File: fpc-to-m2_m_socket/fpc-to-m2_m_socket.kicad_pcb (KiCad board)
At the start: 6 copper layers, 99.3 x 40.6 mm, 31 parts, among them J2 Bus_M.2_Socket_M, J5 Conn_01x02_Pin, Y1 OK2EL89CJI-111YLC-32.768K

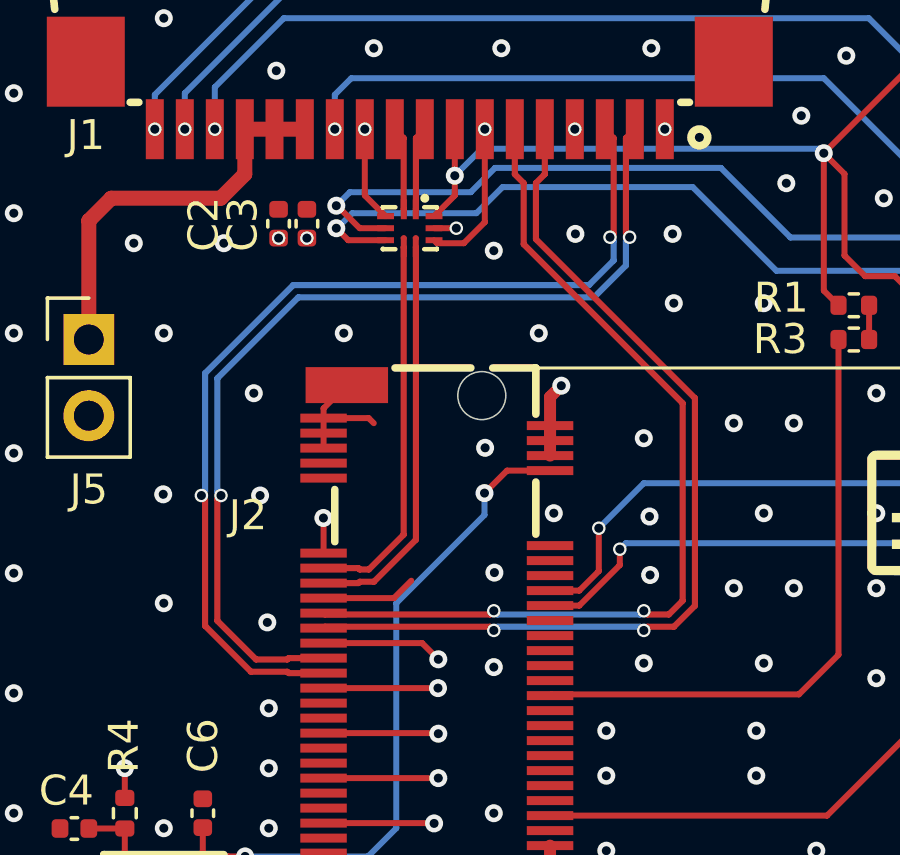
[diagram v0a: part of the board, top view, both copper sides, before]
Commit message: add fillets and skew tuning
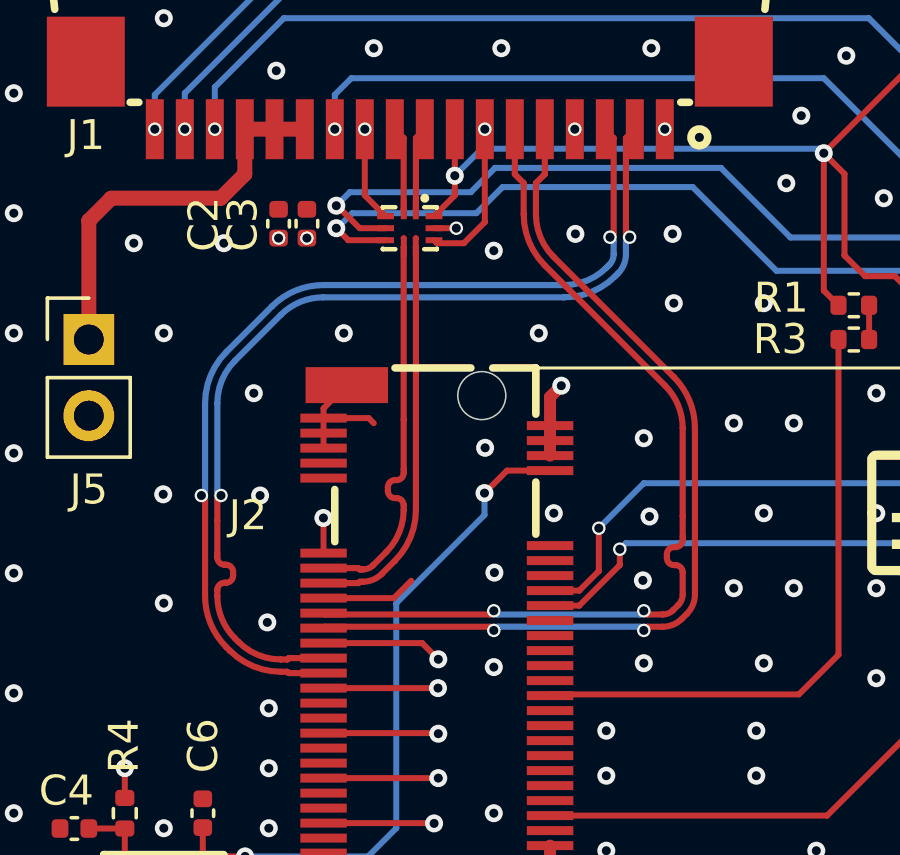
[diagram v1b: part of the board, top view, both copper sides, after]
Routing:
- net PCIe_RX-: track 32.9 -> 32.3 mm

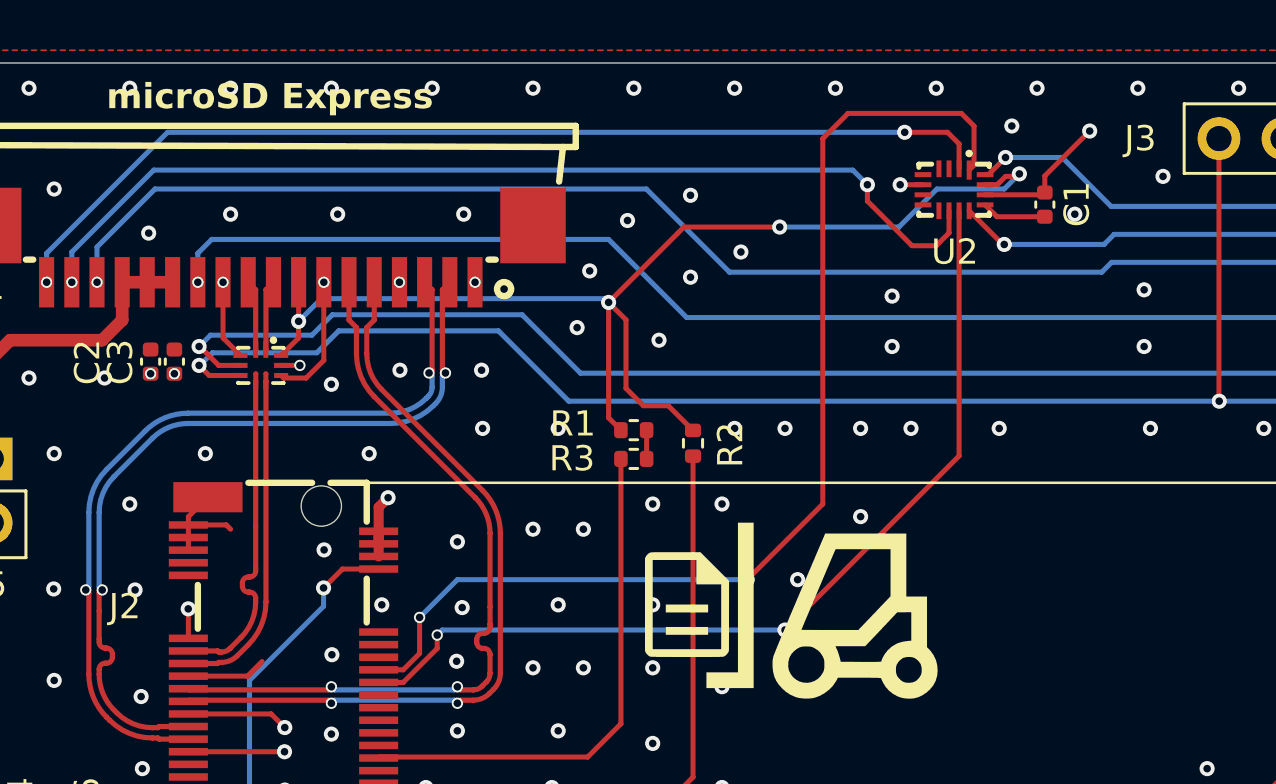
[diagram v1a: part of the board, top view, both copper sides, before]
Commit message: fpc-to-m2_m_socket: switch TMUX1574 to TSSOP-16
The UQFN-16 variant just went out of stock at jlcpcb.
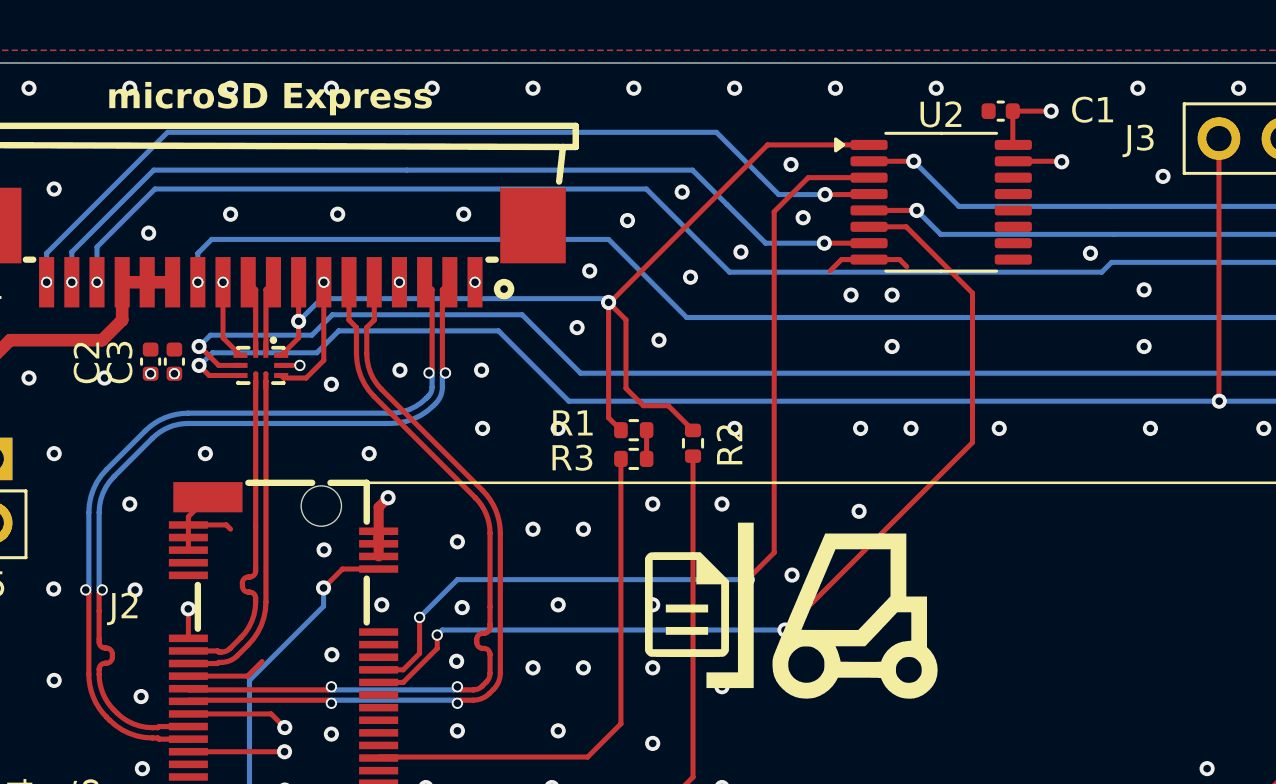
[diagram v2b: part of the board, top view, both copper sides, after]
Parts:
- U2: footprint m1cha:tmux1574 -> Package_SO:TSSOP-16_4.4x5mm_P0.65mm
- moved C1 4.10 mm to (123.6, 75.4), turned to 180 degrees
- moved U2 0.71 mm to (121.2, 79.0), turned to 0 degrees
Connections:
- U2 pad 1: ~{CLKREQ} -> +1V8
- U2 pad 10: ~{PERST}/DAT3/CD -> unconnected-(U2-S3B-Pad10)
- U2 pad 11: ~{PERST} -> unconnected-(U2-S3A-Pad11)
- U2 pad 12: DAT3/CD -> unconnected-(U2-D4-Pad12)
- U2 pad 13: GND -> unconnected-(U2-S4B-Pad13)
- U2 pad 14: +3V3 -> unconnected-(U2-S4A-Pad14)
- U2 pad 15: +1V8 -> GND
- U2 pad 16: DAT2 -> +3V3
- U2 pad 2: ~{CLKREQ}/DAT2 -> DAT2
- U2 pad 3: unconnected-(U2-S2A-Pad3) -> ~{CLKREQ}
- U2 pad 4: unconnected-(U2-S2B-Pad4) -> ~{CLKREQ}/DAT2
- U2 pad 5: unconnected-(U2-D2-Pad5) -> DAT3/CD
- U2 pad 6: GND -> ~{PERST}
- U2 pad 7: unconnected-(U2-D3-Pad7) -> ~{PERST}/DAT3/CD
- U2 pad 8: unconnected-(U2-S3B-Pad8) -> GND
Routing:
- net ~{CLKREQ}: track 44.1 -> 36.3 mm
- net +1V8: track 48.2 -> 41.2 mm, vias 4 -> 2
- net ~{PERST}/DAT3/CD: track 40.1 -> 35.4 mm
- net DAT2: track 57.9 -> 62.2 mm
- net ~{CLKREQ}/DAT2: track 40.5 -> 36.8 mm
- net DAT3/CD: track 59.3 -> 62.9 mm
- net +3V3: track 32.6 -> 29.9 mm
- net ~{PERST}: track 36.8 -> 39.0 mm
- net GND: track 50.9 -> 52.7 mm
